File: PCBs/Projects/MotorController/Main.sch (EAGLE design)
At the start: 25 parts, among them Q1 ZXMP10A17GQ, Q2 BUK9240-100A.118, Q3 BUK9240-100A.118, Q4 MMBT5551LT1G, U1 LT4356-2

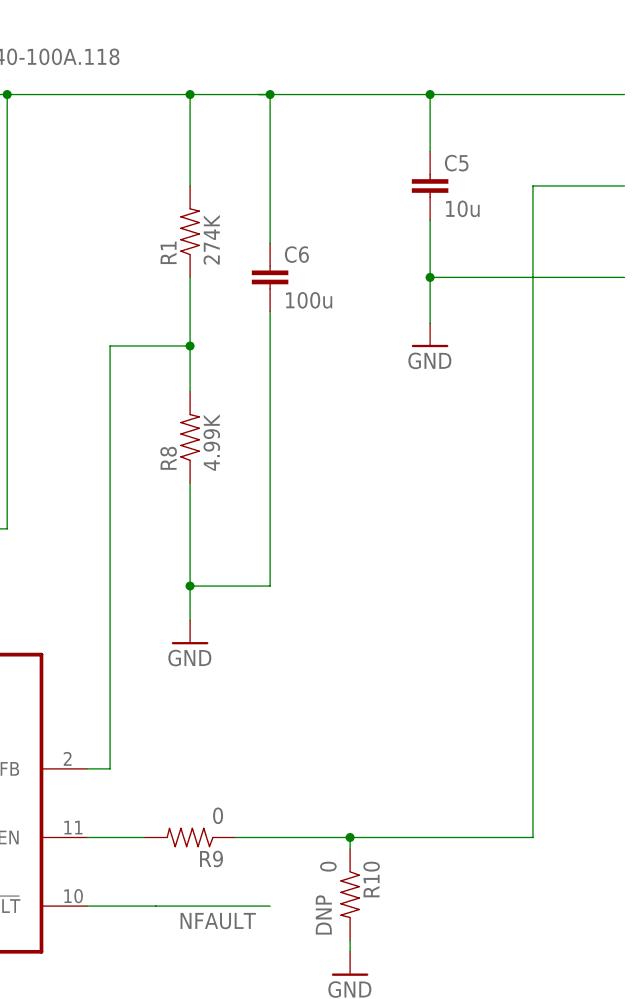
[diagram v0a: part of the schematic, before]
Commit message: Added Board file for gate driver board
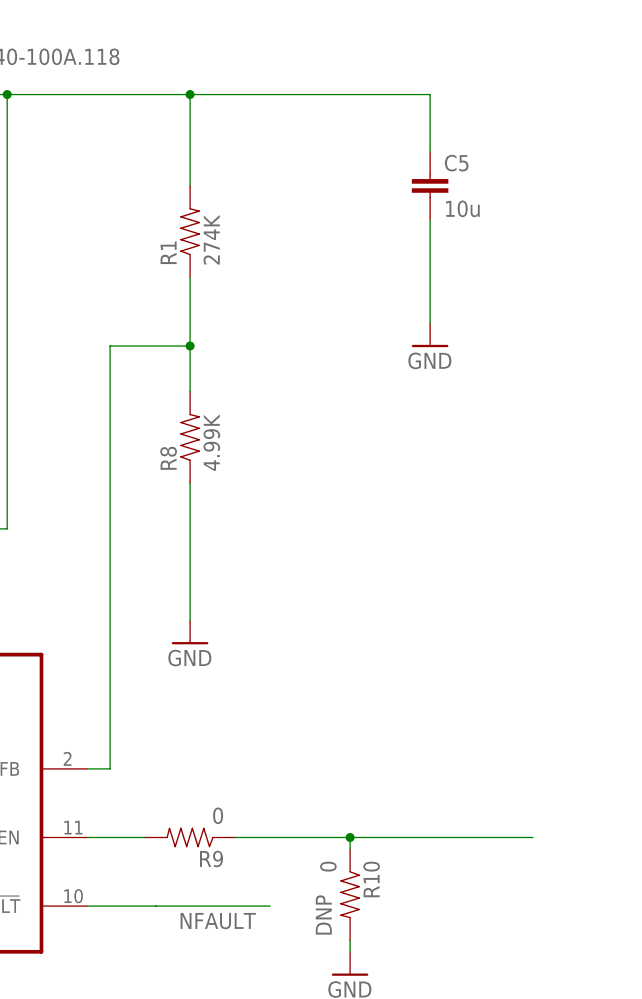
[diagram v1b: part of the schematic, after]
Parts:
- removed C6: 100u, SparkFun-Capacitors:CAP1210
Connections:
- net GND: no longer C6.2
- net N$3: no longer C6.1
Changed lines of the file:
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@@
 <part name="C5" library="SparkFun-Capacitors" deviceset="CAP" device="1210" value="10u"/>
 <part name="GND8" library="SparkFun-Aesthetics" deviceset="GND" device=""/>
-<part name="C6" library="SparkFun-Capacitors" deviceset="CAP" device="1210" value="100u"/>
 <part name="R18" library="SparkFun-Resistors" deviceset="RESISTOR" device="2010" value="51"/>
 <part name="R19" library="SparkFun-Resistors" deviceset="RESISTOR" device="1206" value="30k"/>
@@
 <instance part="C5" gate="G$1" x="63.5" y="68.58"/>
 <instance part="GND8" gate="1" x="63.5" y="52.07"/>
-<instance part="C6" gate="G$1" x="45.72" y="58.42"/>
 <instance part="R18" gate="G$1" x="-111.76" y="52.07"/>
 <instance part="R19" gate="G$1" x="-118.11" y="60.96" smashed="yes" rot="R90">
@@
 <pinref part="GND6" gate="1" pin="GND"/>
 <pinref part="R8" gate="G$1" pin="1"/>
-<wire x1="36.83" y1="21.59" x2="36.83" y2="25.4" width="0.4064" layer="91"/>
-<pinref part="C6" gate="G$1" pin="2"/>
-<wire x1="36.83" y1="25.4" x2="36.83" y2="36.83" width="0.4064" layer="91"/>
-<wire x1="45.72" y1="55.88" x2="45.72" y2="25.4" width="0.4064" layer="91"/>
-<wire x1="45.72" y1="25.4" x2="36.83" y2="25.4" width="0.4064" layer="91"/>
-<junction x="36.83" y="25.4"/>
+<wire x1="36.83" y1="21.59" x2="36.83" y2="36.83" width="0.4064" layer="91"/>
 </segment>
 <segment>
@@
 <segment>
 <pinref part="GND8" gate="1" pin="GND"/>
-<wire x1="85.09" y1="59.69" x2="63.5" y2="59.69" width="0.4064" layer="91"/>
-<wire x1="63.5" y1="59.69" x2="63.5" y2="54.61" width="0.4064" layer="91"/>
 <pinref part="C5" gate="G$1" pin="2"/>
-<wire x1="63.5" y1="59.69" x2="63.5" y2="66.04" width="0.4064" layer="91"/>
-<junction x="63.5" y="59.69"/>
+<wire x1="63.5" y1="54.61" x2="63.5" y2="66.04" width="0.4064" layer="91"/>
 </segment>
 <segment>
@@
 <wire x1="36.83" y1="80.01" x2="36.83" y2="69.85" width="0.4064" layer="91"/>
 <junction x="16.51" y="80.01"/>
-<pinref part="C6" gate="G$1" pin="1"/>
-<wire x1="45.72" y1="63.5" x2="45.72" y2="80.01" width="0.4064" layer="91"/>
-<wire x1="45.72" y1="80.01" x2="36.83" y2="80.01" width="0.4064" layer="91"/>
 <junction x="36.83" y="80.01"/>
 <pinref part="C5" gate="G$1" pin="1"/>
-<wire x1="85.09" y1="80.01" x2="63.5" y2="80.01" width="0.4064" layer="91"/>
 <wire x1="63.5" y1="80.01" x2="63.5" y2="73.66" width="0.4064" layer="91"/>
-<wire x1="63.5" y1="80.01" x2="45.72" y2="80.01" width="0.4064" layer="91"/>
-<junction x="45.72" y="80.01"/>
-<wire x1="45.72" y1="80.01" x2="44.45" y2="80.01" width="0.4064" layer="91"/>
-<junction x="63.5" y="80.01"/>
+<wire x1="63.5" y1="80.01" x2="36.83" y2="80.01" width="0.4064" layer="91"/>
 <pinref part="U1" gate="U1" pin="OUT"/>
 <wire x1="10.16" y1="22.86" x2="10.16" y2="31.75" width="0.4064" layer="91"/>
@@
 <net name="N$15" class="0">
 <segment>
-<wire x1="85.09" y1="69.85" x2="74.93" y2="69.85" width="0.4064" layer="91"/>
-<wire x1="74.93" y1="-2.54" x2="74.93" y2="69.85" width="0.4064" layer="91"/>
 <pinref part="R9" gate="G$1" pin="1"/>
 <wire x1="41.91" y1="-2.54" x2="54.61" y2="-2.54" width="0.4064" layer="91"/>

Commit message: RepoFix
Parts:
- added C6: 100u, SparkFun-Capacitors:CAP1210
- added D3: 1N4148W-7-F, SparkFun-DiscreteSemi:DIODESOD123
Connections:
- removed net N$10: Q2.G, R2.2
- removed net N$21: D9.C, R20.2
- removed net N$7: R3.2, R4.1, U1.GATE
- new net N$16: D3.C, R20.2
- new net N$17: U1.SNS
- new net N$4: D3.A, D9.C
- net GND: now also C6.2
- net N$12: no longer D2.C, Q1.S, R17.1, R19.2
- net N$3: now also C6.1; no longer Q3.D, U1.OUT
- net N$5: now also U1.OUT; no longer Q2.S, Q3.S
- net N$6: now also D2.C, Q1.S, R19.2; no longer Q4.C, R2.1, R3.1
- net N$8: no longer Q2.D, R17.2, U1.SNS
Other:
- moved on the sheet: D1, D2, D9, Q1, Q2, Q3, Q4, R17, R18, R19, R2, R20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

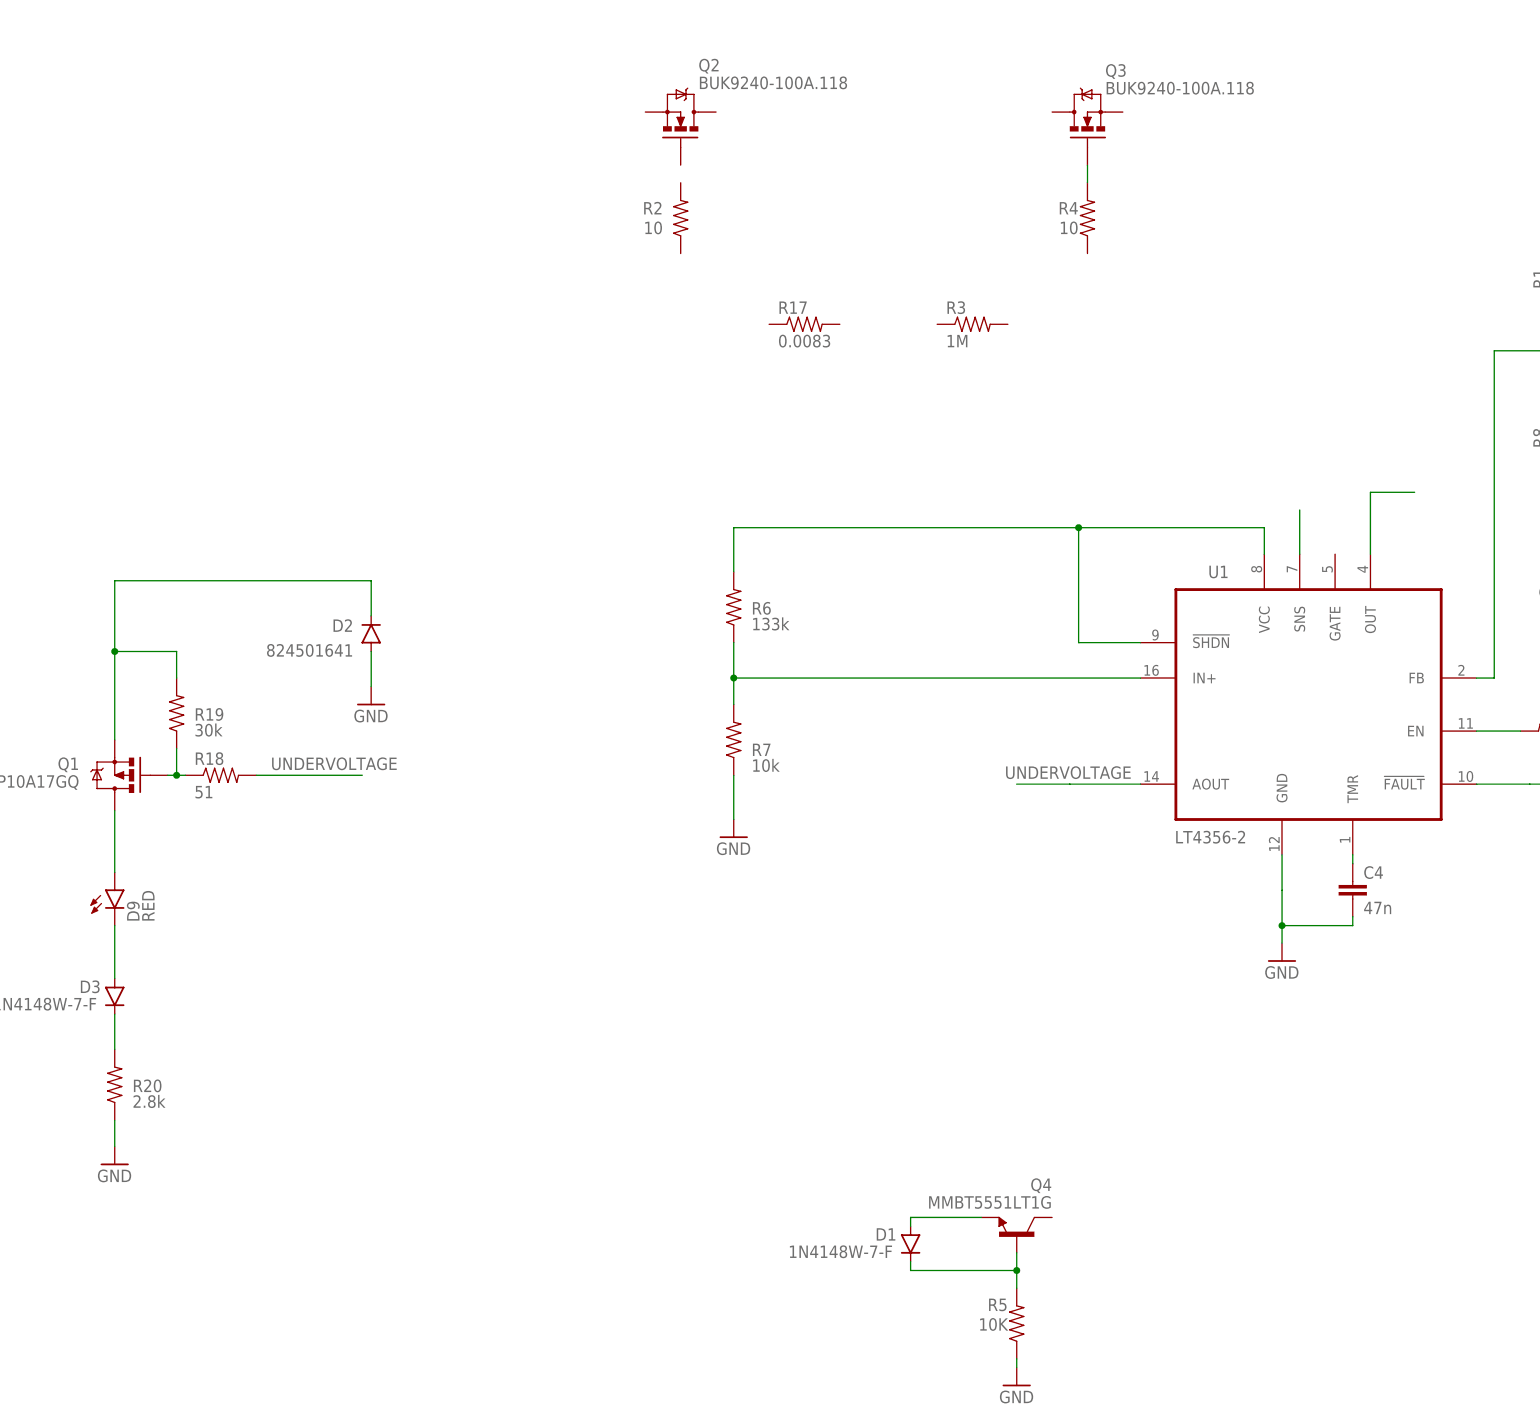
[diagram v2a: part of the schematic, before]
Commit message: Added Parts, work on power input protection
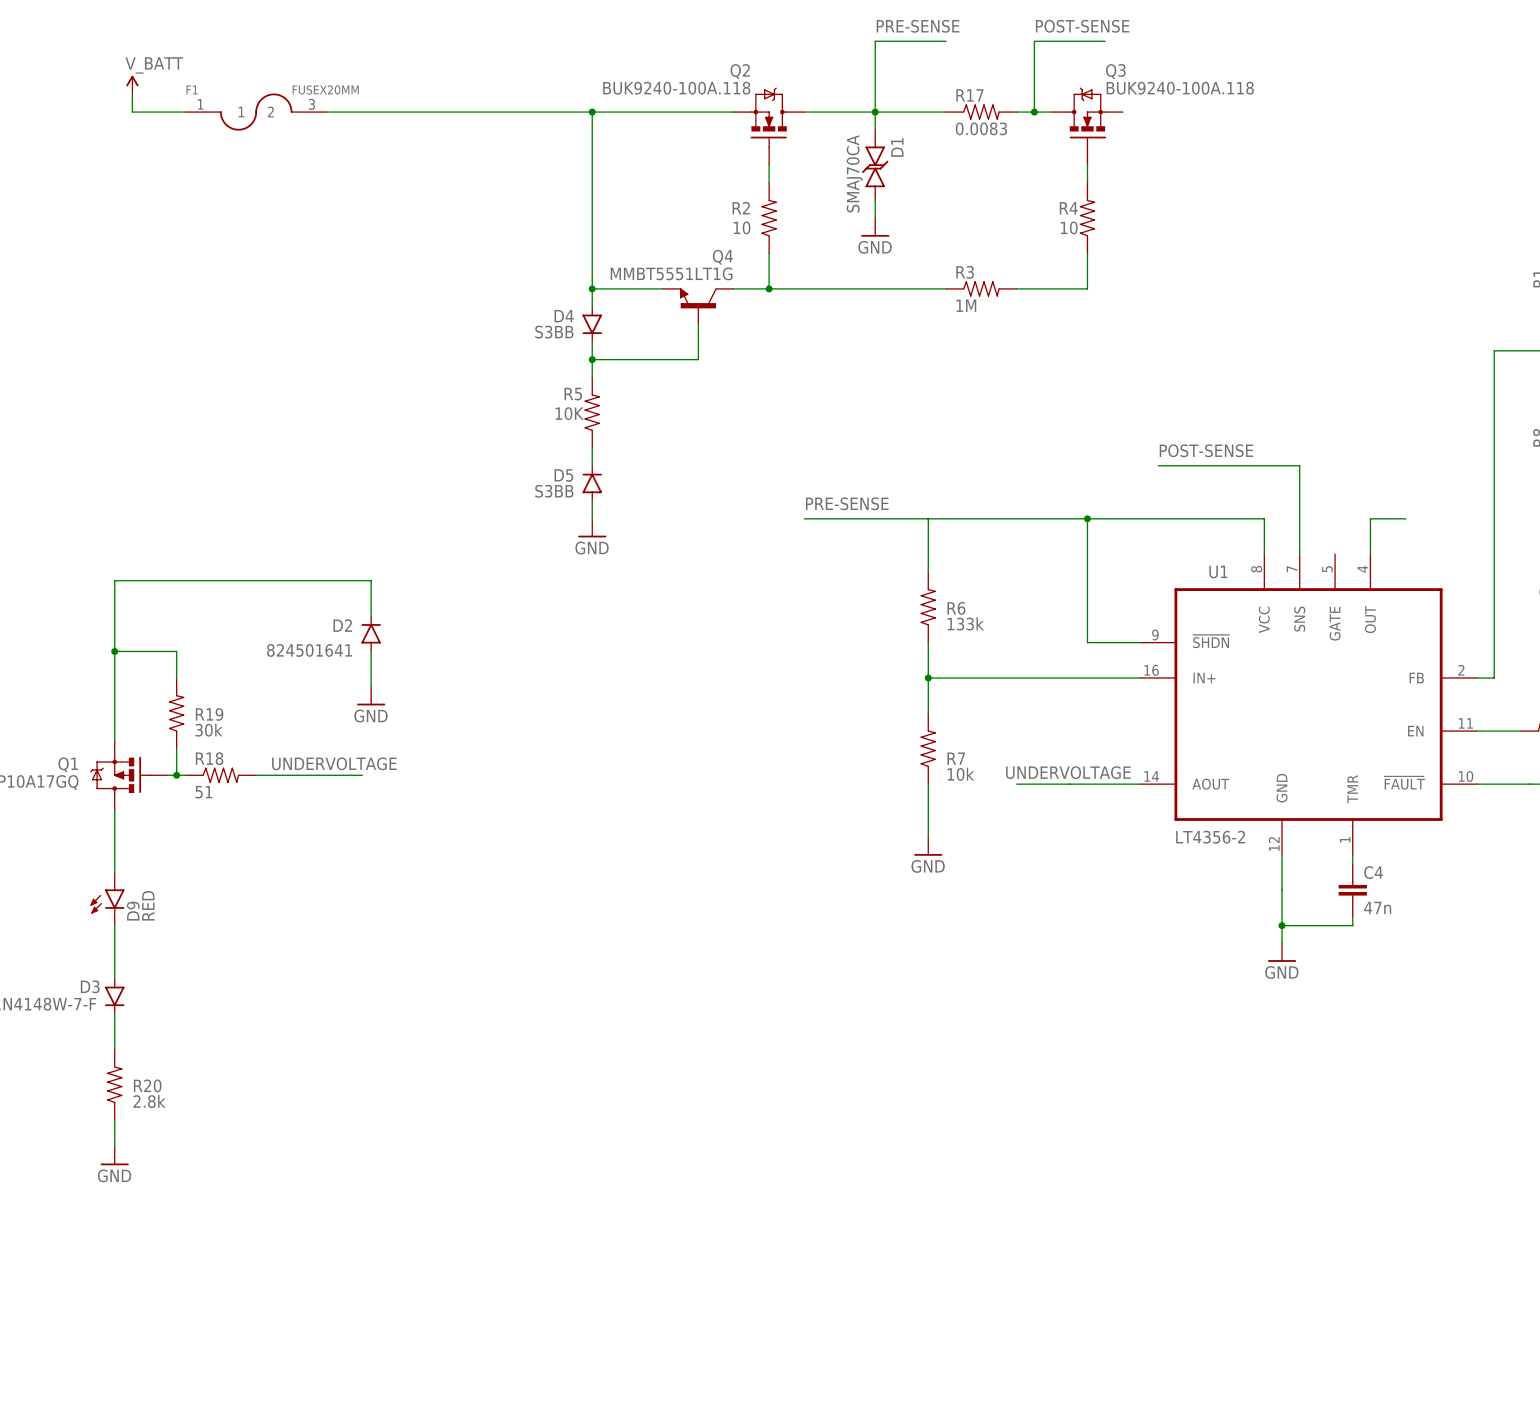
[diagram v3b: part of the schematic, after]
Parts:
- added D4, D5: S3BB, SparkFun-DiscreteSemi:DIODES3BB
- added F1: FUSEX20MM, SparkFun-Passives:FUSEX20MM
- D1: value 1N4148W-7-F -> SMAJ70CA; device SparkFun-DiscreteSemi:DIODESOD123 -> SparkFun-DiscreteSemi:SMAJ70CA
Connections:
- removed net N$12: R6.2, U1.!SHDN, U1.VCC
- removed net N$17: U1.SNS
- new net N$20: Q4.C, R2.1, R3.1
- new net N$21: R3.2, R4.1
- new net N$23: D5.C, R5.1
- new net N$7: Q2.G, R2.2
- new net POST-SENSE: Q3.D, R17.2, U1.SNS
- new net PRE-SENSE: D1.A, Q2.D, R17.1, R6.2, U1.!SHDN, U1.VCC
- new net V_BATT: F1.1
- net GND: now also D1.C, D5.A; no longer R5.1
- net N$8: now also D4.A, F1.2, Q2.S; no longer D1.A
- net N$9: now also D4.C; no longer D1.C
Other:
- moved on the sheet: Q2, Q4, R17, R2, R3, R5, R6, R7
